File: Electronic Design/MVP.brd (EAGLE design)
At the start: 94.5 x 68.7 mm, 35 parts, among them IC1 ACS712ELC-5A, IC2 ATMEGA328-PU, Q1 IRF9540, Q2 IRF9540, X1 16MHz

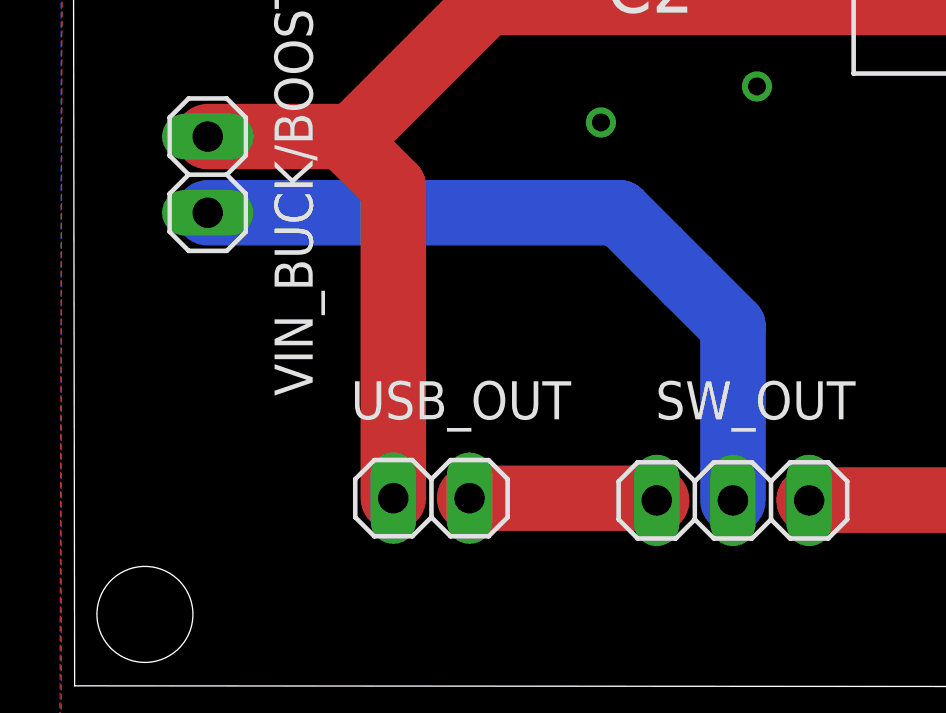
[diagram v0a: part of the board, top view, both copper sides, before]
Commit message: connected VIN_BUCK/BOOST -ve to ground
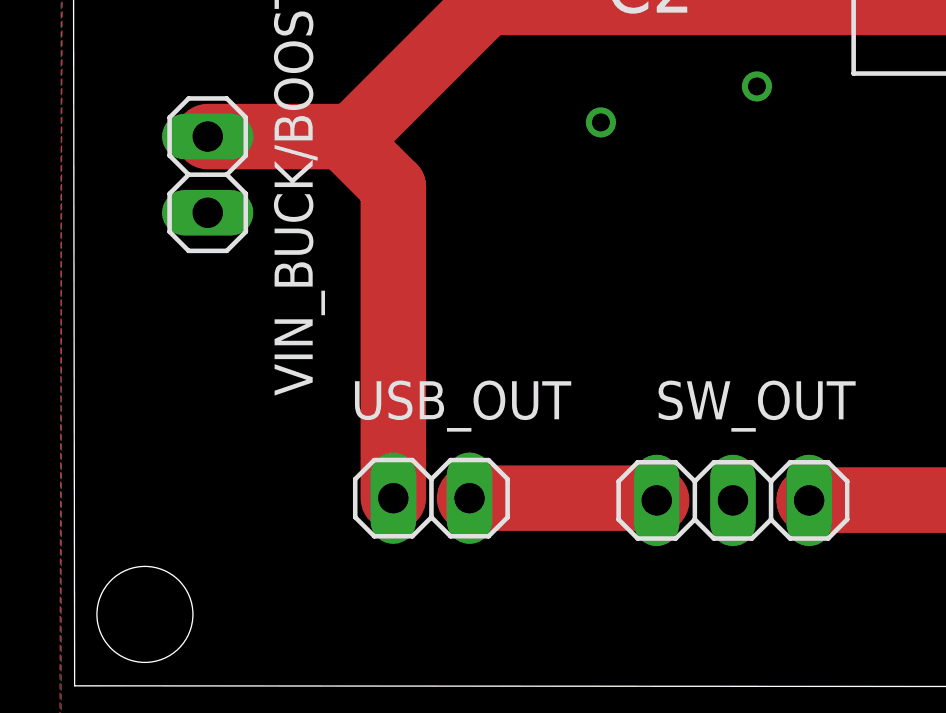
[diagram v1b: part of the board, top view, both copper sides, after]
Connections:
- removed net N$22: SW_OUT.2, VIN_BUCK/BOOST.2
- net GND: now also SW_OUT.2, VIN_BUCK/BOOST.2
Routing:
- net N$22: track 24.9 -> 0.00 mm
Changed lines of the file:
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@@
 <setting verticaltext="up"/>
 </settings>
-<grid distance="0.2" unitdist="mm" unit="mm" style="lines" multiple="1" display="no" altdistance="0.025" altunitdist="inch" altunit="mm"/>
+<grid distance="0.003125" unitdist="mic" unit="mm" style="lines" multiple="1" display="no" altdistance="0.025" altunitdist="inch" altunit="mm"/>
 <layers>
 <layer number="1" name="Top" color="4" fill="1" visible="yes" active="yes"/>
@@
 <contactref element="VOUT-" pad="2"/>
 <contactref element="VIN_BUCK" pad="2"/>
+<contactref element="SW_OUT" pad="2"/>
+<contactref element="VIN_BUCK/BOOST" pad="2"/>
 </signal>
 <signal name="N$19">
@@
 <wire x1="80.174278125" y1="36.6" x2="79.500690625" y2="36.5735875" width="0.6096" layer="1"/>
 </signal>
-<signal name="N$22">
-<contactref element="SW_OUT" pad="2"/>
-<wire x1="20.28176875" y1="27.51823125" x2="21.3" y2="26.5" width="2.1844" layer="16"/>
-<wire x1="21.3" y1="26.5" x2="22.8" y2="25" width="2.1844" layer="16"/>
-<wire x1="22.8" y1="25" x2="22.8" y2="19.2" width="2.1844" layer="16"/>
-<contactref element="VIN_BUCK/BOOST" pad="2"/>
-<wire x1="5.29299375" y1="28.78823125" x2="19.01176875" y2="28.78823125" width="2.1844" layer="16"/>
-<wire x1="19.01176875" y1="28.78823125" x2="20.28176875" y2="27.51823125" width="2.1844" layer="16"/>
-</signal>
 <signal name="N$23">

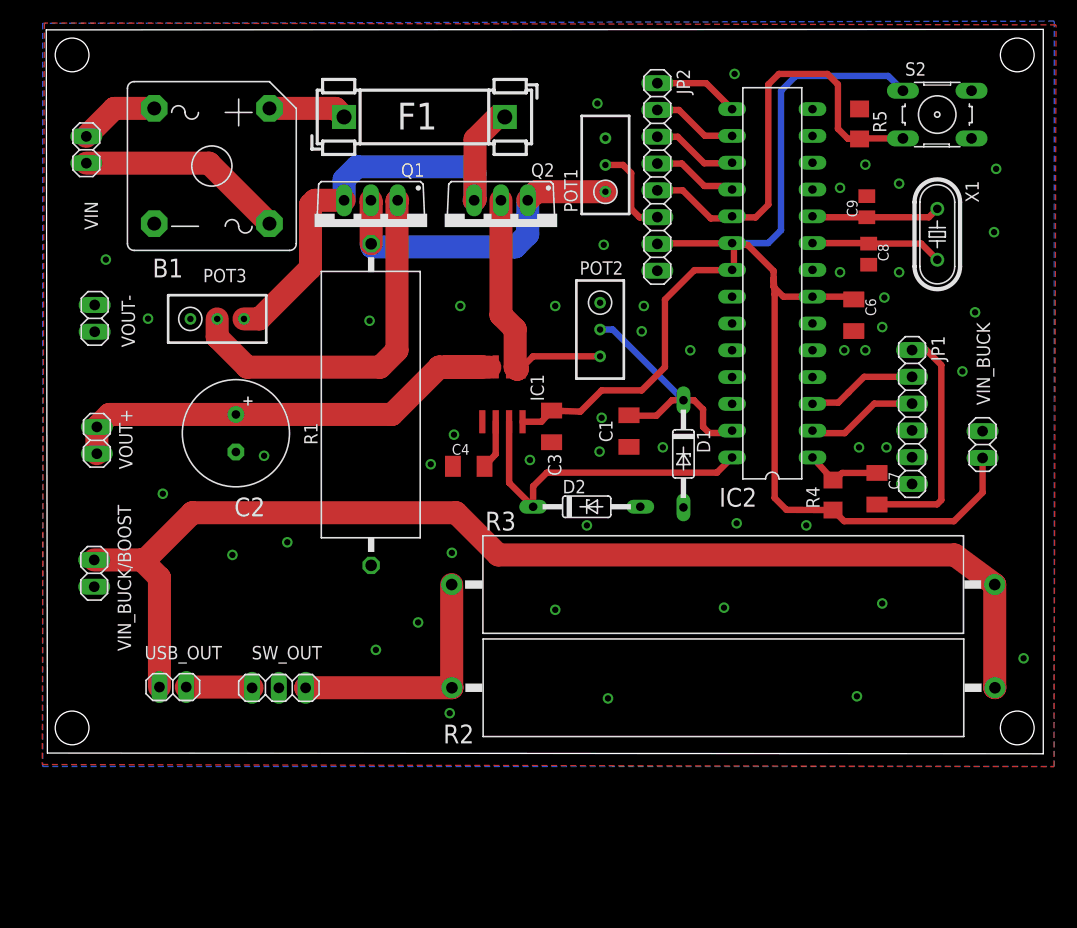
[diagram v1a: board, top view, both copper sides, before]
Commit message: Rerouting PCB to fit the enclosure being ordered. Holes placed so that they will fit over enclosure holes
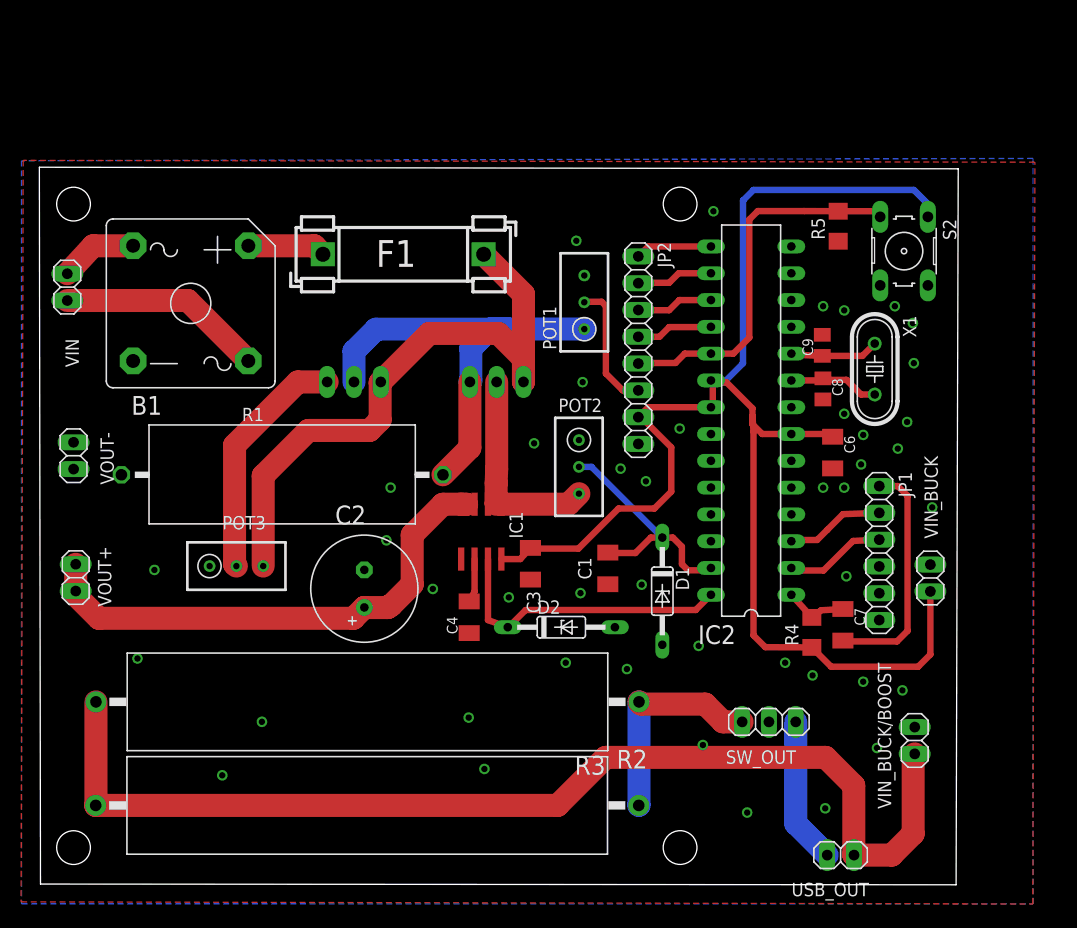
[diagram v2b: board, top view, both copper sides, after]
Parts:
- moved VIN_BUCK/BOOST 79.4 mm to (83.1, 14.2), turned to 90 degrees
- moved USB_OUT 65.3 mm to (76.1, 3.35), turned to 180 degrees
- moved SW_OUT 46.6 mm to (69.3, 16.0), turned to 180 degrees
- moved R2 35.6 mm to (31.2, 8.06), turned to 180 degrees
- moved R3 35.5 mm to (31.2, 17.9), turned to 180 degrees
- moved POT3 23.5 mm to (18.8, 30.7)
- moved C2 19.1 mm to (30.9, 28.6), turned to 90 degrees
- moved Q1 17.3 mm to (29.9, 45.7), flipped to the bottom
- moved Q2 17.2 mm to (43.5, 45.7), flipped to the bottom
- moved JP2 16.5 mm to (56.9, 51.2)
- moved C4 14.3 mm to (40.8, 25.9), turned to 90 degrees
- moved X1 14.1 mm to (79.3, 49.4)
- moved C9 13.8 mm to (74.3, 51.7)
- moved VIN_BUCK 13.6 mm to (84.6, 29.6)
- moved C8 13.5 mm to (74.4, 47.5)
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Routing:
- net N$10: track 44.9 -> 57.8 mm
- net N$35: track 30.6 -> 43.1 mm
- net N$7: track 34.9 -> 22.8 mm
- net N$25: track 6.27 -> 13.9 mm
- net N$23: track 112.3 -> 105.4 mm
- net N$8: track 41.9 -> 35.7 mm
- net N$3: track 26.4 -> 20.7 mm
- net +5V: track 130.8 -> 135.9 mm
- net N$16: track 13.1 -> 8.62 mm
- net N$15: track 12.2 -> 8.43 mm
- net OVERV: track 8.98 -> 12.4 mm
- net N$24: track 23.7 -> 20.4 mm
- net M1S: track 46.2 -> 48.9 mm
- net IIN: track 30.9 -> 28.3 mm
- net N$17: track 7.29 -> 6.07 mm
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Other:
- board size 94.5 x 68.7 mm -> 87.1 x 68 mm

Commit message: Removed dimensions and cleared remaining DRC errors (mainly overlap from stray vias
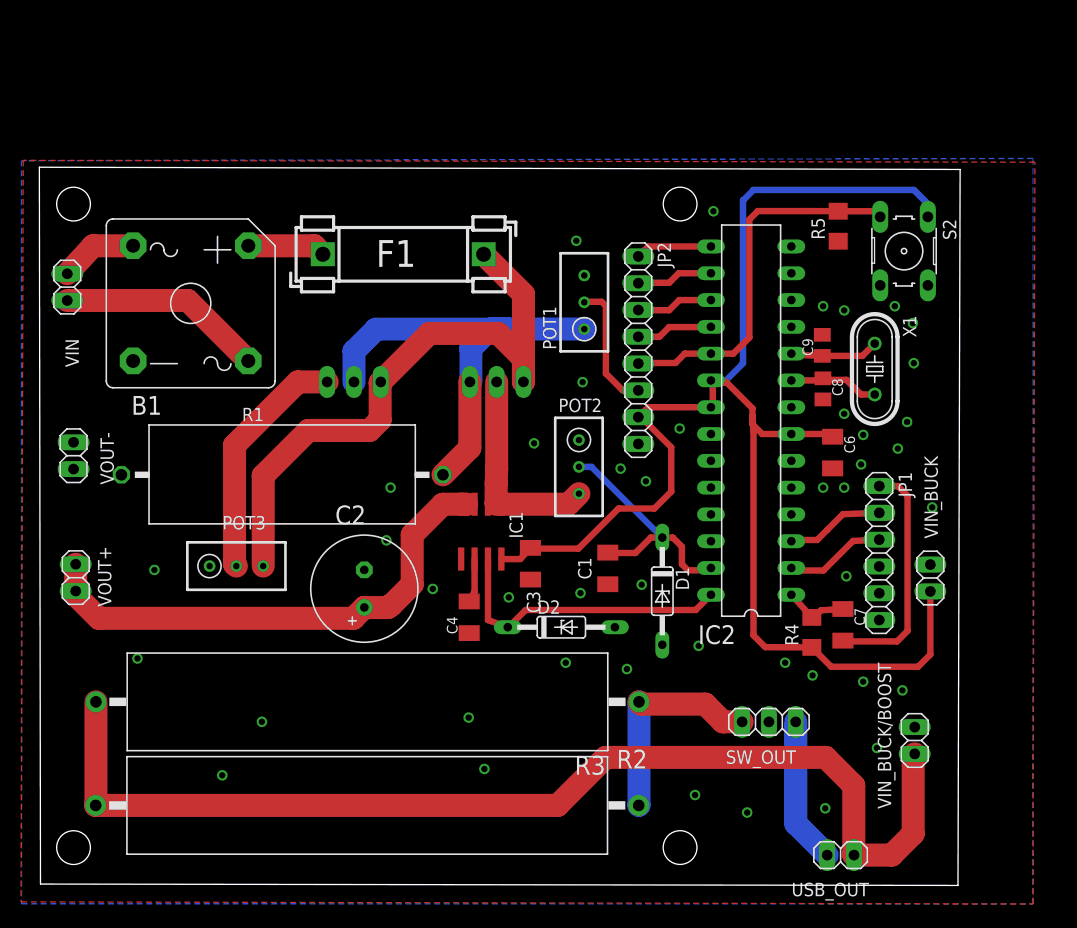
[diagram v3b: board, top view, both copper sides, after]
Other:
- board size 87.1 x 68 mm -> 87.3 x 68.1 mm
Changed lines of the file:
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@@
 <board>
 <plain>
-<wire x1="0.202675" y1="0.5995125" x2="87.0011375" y2="0.5293875" width="0" layer="20"/>
-<wire x1="87.0011375" y1="0.5293875" x2="87.203640625" y2="68.40416875" width="0" layer="20"/>
-<wire x1="87.203640625" y1="68.40416875" x2="0.096228125" y2="68.55409375" width="0" layer="20"/>
+<wire x1="0.202675" y1="0.5995125" x2="87.1811375" y2="0.4693875" width="0" layer="20"/>
+<wire x1="87.1811375" y1="0.4693875" x2="87.383640625" y2="68.34416875" width="0" layer="20"/>
+<wire x1="87.383640625" y1="68.34416875" x2="0.096228125" y2="68.55409375" width="0" layer="20"/>
 <wire x1="0.096228125" y1="68.55409375" x2="0.202675" y2="0.5995125" width="0" layer="20"/>
 <hole x="3.33508125" y="65.059571875" drill="3.2"/>
@@
 <hole x="60.835490625" y="4.0602" drill="3.2"/>
 <hole x="3.33523125" y="4.0560375" drill="3.2"/>
-<dimension x1="3.33508125" y1="65.059571875" x2="3.33523125" y2="4.0560375" x3="-23.98" y3="34.557803125" textsize="1.778" layer="1" dtype="vertical" precision="6"/>
-<dimension x1="60.839146875" y1="65.06315" x2="60.835490625" y2="4.0602" x3="103.46" y3="34.561675" textsize="1.778" layer="1" dtype="vertical" precision="6"/>
-<dimension x1="3.33523125" y1="4.0560375" x2="60.835490625" y2="4.0602" x3="32.085359375" y3="-13" textsize="1.778" layer="1" dtype="horizontal" precision="6"/>
-<dimension x1="3.33508125" y1="65.059571875" x2="60.839146875" y2="65.06315" x3="32.0871125" y3="75.23" textsize="1.778" layer="1" dtype="horizontal" precision="6"/>
 </plain>
 <attributes>
@@
 <via x="17.43569375" y="10.9102" extent="1-16" drill="0.6" shape="square"/>
 <via x="78.19569375" y="19.7802" extent="1-16" drill="0.6" shape="square"/>
-<via x="62.99569375" y="13.7802" extent="1-16" drill="0.6" shape="square"/>
+<via x="62.25569375" y="9.0402" extent="1-16" drill="0.6" shape="square"/>
 <via x="84.736575" y="36.30315" extent="1-16" drill="0.6" shape="square"/>
 <via x="82.359228125" y="44.404675" extent="1-16" drill="0.6" shape="square"/>

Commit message: widening board to accomodate pin header on left hand side
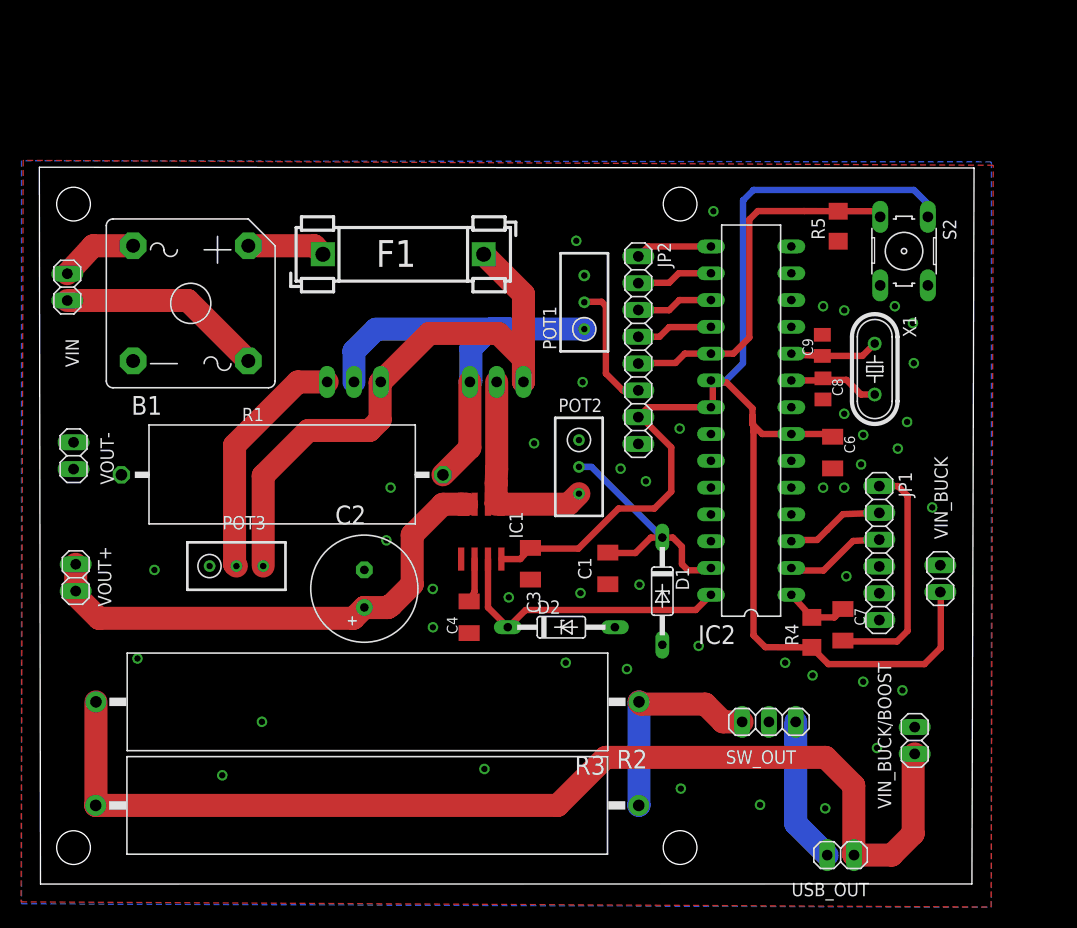
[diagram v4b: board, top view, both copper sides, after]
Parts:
- moved VIN_BUCK 0.94 mm to (85.5, 29.6)
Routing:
- net IIN: track 28.3 -> 27.8 mm
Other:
- board size 87.3 x 68.1 mm -> 88.6 x 68 mm
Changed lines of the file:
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@@
 <board>
 <plain>
-<wire x1="0.202675" y1="0.5995125" x2="87.1811375" y2="0.4693875" width="0" layer="20"/>
-<wire x1="87.1811375" y1="0.4693875" x2="87.383640625" y2="68.34416875" width="0" layer="20"/>
-<wire x1="87.383640625" y1="68.34416875" x2="0.096228125" y2="68.55409375" width="0" layer="20"/>
+<wire x1="0.202675" y1="0.5995125" x2="88.5011375" y2="0.6093875" width="0" layer="20"/>
+<wire x1="88.5011375" y1="0.6093875" x2="88.703640625" y2="68.48416875" width="0" layer="20"/>
+<wire x1="88.703640625" y1="68.48416875" x2="0.096228125" y2="68.55409375" width="0" layer="20"/>
 <wire x1="0.096228125" y1="68.55409375" x2="0.202675" y2="0.5995125" width="0" layer="20"/>
 <hole x="3.33508125" y="65.059571875" drill="3.2"/>
@@
 <attribute name="VALUE" x="6.51230625" y="37.3968625" size="1.27" layer="27" rot="R90"/>
 </element>
-<element name="VIN_BUCK" library="pinhead" package="1X02" value="" x="84.56119375" y="29.614190625" rot="R90"/>
+<element name="VIN_BUCK" library="pinhead" package="1X02" value="" x="85.50119375" y="29.554190625" rot="R90"/>
 <element name="JP1" library="pinhead" package="1X06" value="" x="79.718590625" y="31.978721875" rot="R270"/>
 <element name="C6" library="resistor" package="C1206K" value="10u" x="75.29648125" y="41.50599375" rot="R270"/>
@@
 <contactref element="IC1" pad="7"/>
 <contactref element="IC2" pad="28"/>
-<wire x1="42.62365625" y1="31.4083875" x2="42.62365625" y2="25.624196875" width="0.6096" layer="1"/>
-<wire x1="42.62365625" y1="25.624196875" x2="44.49920625" y2="24.948646875" width="0.6096" layer="1"/>
 <wire x1="44.49920625" y1="24.948646875" x2="44.89920625" y2="25.2837125" width="0.6096" layer="1"/>
 <wire x1="44.89920625" y1="25.2837125" x2="46.19569375" y2="26.5802" width="0.6096" layer="1"/>
 <wire x1="46.19569375" y1="26.5802" x2="62.319809375" y2="26.5802" width="0.6096" layer="1"/>
 <wire x1="62.319809375" y1="26.5802" x2="63.7625375" y2="28.022928125" width="0.6096" layer="1"/>
+<wire x1="42.62365625" y1="31.4083875" x2="42.62365625" y2="26.824196875" width="0.6096" layer="1"/>
+<wire x1="42.62365625" y1="26.824196875" x2="44.49920625" y2="24.948646875" width="0.6096" layer="1"/>
 </signal>
 <signal name="GND">
@@
 <vertex x="-1.43555" y="69.20553125"/>
 <vertex x="-1.63555" y="-1.08879375"/>
-<vertex x="94.272990625" y="-1.28879375"/>
-<vertex x="94.472990625" y="69.029465625"/>
+<vertex x="90.322990625" y="-1.57879375"/>
+<vertex x="90.522990625" y="68.739465625"/>
 </polygon>
 <polygon width="0.6096" layer="16" isolate="0.3">
 <vertex x="-1.594540625" y="69.169190625"/>
 <vertex x="-1.594540625" y="-1.27125625"/>
-<vertex x="94.29690625" y="-1.27125625"/>
-<vertex x="94.29690625" y="69.388053125"/>
+<vertex x="90.34690625" y="-1.60125625"/>
+<vertex x="90.34690625" y="69.058053125"/>
 </polygon>
 <via x="44.59569375" y="27.7802" extent="1-16" drill="0.6" shape="square"/>
 <via x="51.39569375" y="28.1802" extent="1-16" drill="0.6" shape="square"/>
-<via x="57.19569375" y="28.9802" extent="1-16" drill="0.6" shape="square"/>
+<via x="56.98569375" y="28.9802" extent="1-16" drill="0.6" shape="square"/>
 <via x="57.59569375" y="38.7802" extent="1-16" drill="0.6" shape="square"/>
 <via x="62.59569375" y="23.1802" extent="1-16" drill="0.6" shape="square"/>
@@
 <via x="42.28569375" y="11.5102" extent="1-16" drill="0.6" shape="square"/>
 <via x="73.39569375" y="20.3802" extent="1-16" drill="0.6" shape="square"/>
-<via x="67.19569375" y="7.3802" extent="1-16" drill="0.6" shape="square"/>
-<via x="40.79569375" y="16.3802" extent="1-16" drill="0.6" shape="square"/>
+<via x="68.41569375" y="8.1102" extent="1-16" drill="0.6" shape="square"/>
+<via x="37.40569375" y="24.9402" extent="1-16" drill="0.6" shape="square"/>
 <via x="17.43569375" y="10.9102" extent="1-16" drill="0.6" shape="square"/>
 <via x="78.19569375" y="19.7802" extent="1-16" drill="0.6" shape="square"/>
-<via x="62.25569375" y="9.0402" extent="1-16" drill="0.6" shape="square"/>
+<via x="60.90569375" y="9.6502" extent="1-16" drill="0.6" shape="square"/>
 <via x="84.736575" y="36.30315" extent="1-16" drill="0.6" shape="square"/>
 <via x="82.359228125" y="44.404675" extent="1-16" drill="0.6" shape="square"/>
@@
 <wire x1="67.79569375" y1="24.1802" x2="67.79569375" y2="43.481478125" width="0.6096" layer="1"/>
 <wire x1="67.79569375" y1="43.481478125" x2="67.696971875" y2="44.9802" width="0.6096" layer="1"/>
-<wire x1="84.56119375" y1="28.344190625" x2="84.56119375" y2="22.36119375" width="0.6096" layer="1"/>
-<wire x1="84.56119375" y1="22.36119375" x2="83.4" y2="21.2" width="0.6096" layer="1"/>
-<wire x1="83.4" y1="21.2" x2="75.162578125" y2="21.2" width="0.6096" layer="1"/>
-<wire x1="75.162578125" y1="21.2" x2="73.328209375" y2="23.03436875" width="0.6096" layer="1"/>
 <wire x1="63.7625375" y1="45.802928125" x2="57.814984375" y2="45.802928125" width="0.6096" layer="1"/>
 <wire x1="57.814984375" y1="45.802928125" x2="56.8750375" y2="44.86298125" width="0.6096" layer="1"/>
@@
 <wire x1="65" y1="48.169528125" x2="63.9359375" y2="48.169528125" width="0.6096" layer="16"/>
 <wire x1="63.9359375" y1="48.169528125" x2="63.7625375" y2="48.342928125" width="0.6096" layer="16"/>
+<wire x1="73.328209375" y1="23.03436875" x2="73.328209375" y2="23.011790625" width="0.6096" layer="1"/>
+<wire x1="73.328209375" y1="23.011790625" x2="74.89" y2="21.45" width="0.6096" layer="1"/>
+<wire x1="74.89" y1="21.45" x2="84" y2="21.45" width="0.6096" layer="1"/>
+<wire x1="84" y1="21.45" x2="85.55" y2="23" width="0.6096" layer="1"/>
+<wire x1="85.55" y1="23" x2="85.55" y2="28.235384375" width="0.6096" layer="1"/>
+<wire x1="85.55" y1="28.235384375" x2="85.50119375" y2="28.284190625" width="0.6096" layer="1"/>
 </signal>
 <signal name="N$1">
@@
 <wire x1="73.328209375" y1="25.87836875" x2="71.528209375" y2="27.87725625" width="0.6096" layer="1"/>
 <wire x1="71.528209375" y1="27.87725625" x2="71.3825375" y2="28.022928125" width="0.6096" layer="1"/>
-<wire x1="76.269071875" y1="26.6767375" x2="74.203628125" y2="26.5537875" width="0.6096" layer="1"/>
-<wire x1="74.203628125" y1="26.5537875" x2="73.328209375" y2="25.87836875" width="0.6096" layer="1"/>
+<wire x1="73.328209375" y1="25.87836875" x2="75.470703125" y2="25.87836875" width="0.6096" layer="1"/>
+<wire x1="75.470703125" y1="25.87836875" x2="76.269071875" y2="26.6767375" width="0.6096" layer="1"/>
 </signal>
 <signal name="N$8">
